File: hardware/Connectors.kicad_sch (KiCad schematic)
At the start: 6 parts, among them J2 Conn_02x20_Odd_Even, J3 M80-8420445, J4 M80-8661022, U1 AS222-35PN-933

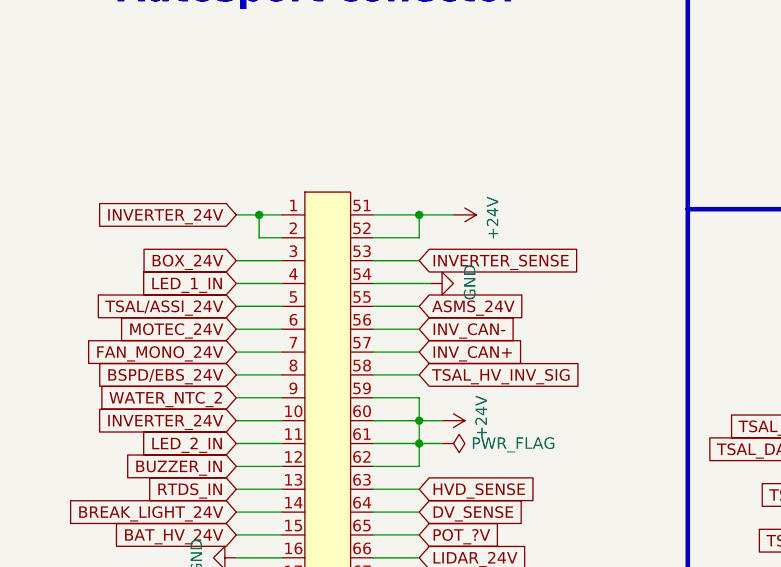
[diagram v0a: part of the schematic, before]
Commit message: nameing scheme update
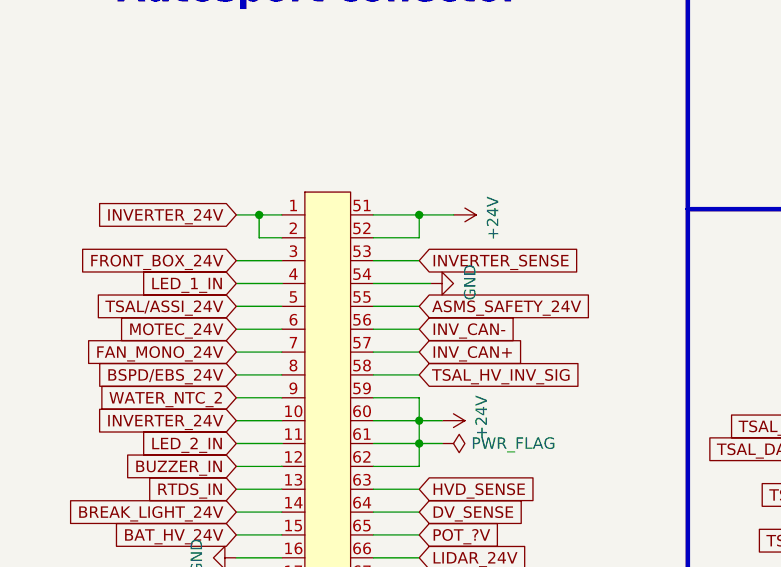
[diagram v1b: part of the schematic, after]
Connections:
- net ASMS_24V renamed ASMS_SAFETY_24V
- net BOX_24V renamed FRONT_BOX_24V
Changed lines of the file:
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@@
     )
   )
-  (global_label "BOX_24V" (shape input) (at 43.18 57.15 180) (fields_autoplaced)
+  (global_label "FRONT_BOX_24V" (shape input) (at 43.18 57.15 180) (fields_autoplaced)
     (effects (font (size 1.27 1.27)) (justify right))
-    (property "Intersheet References" "${INTERSHEET_REFS}" (id 0) (at 32.5706 57.0706 0)
+    (property "Intersheet References" "${INTERSHEET_REFS}" (id 0) (at 25.6158 57.0706 0)
       (effects (font (size 1.27 1.27)) (justify right) hide)
     )
@@
     )
   )
-  (global_label "ASMS_24V" (shape input) (at 63.5 62.23 0) (fields_autoplaced)
+  (global_label "ASMS_SAFETY_24V" (shape input) (at 63.5 62.23 0) (fields_autoplaced)
     (effects (font (size 1.27 1.27)) (justify left))
-    (property "Intersheet References" "${INTERSHEET_REFS}" (id 0) (at 75.2585 62.1506 0)
+    (property "Intersheet References" "${INTERSHEET_REFS}" (id 0) (at 82.818 62.1506 0)
       (effects (font (size 1.27 1.27)) (justify left) hide)
     )
